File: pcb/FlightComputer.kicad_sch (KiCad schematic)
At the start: 79 parts, among them J1 USB4105-GF-A, J2 MOTOR L, J3 MOTOR R, J4 LED L, J7 SERVO R, J8 SERVO R, Q1 DMG3415U, Q2 Si2319CDS, Q3 Si2319CDS, Q4 MMBT3904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

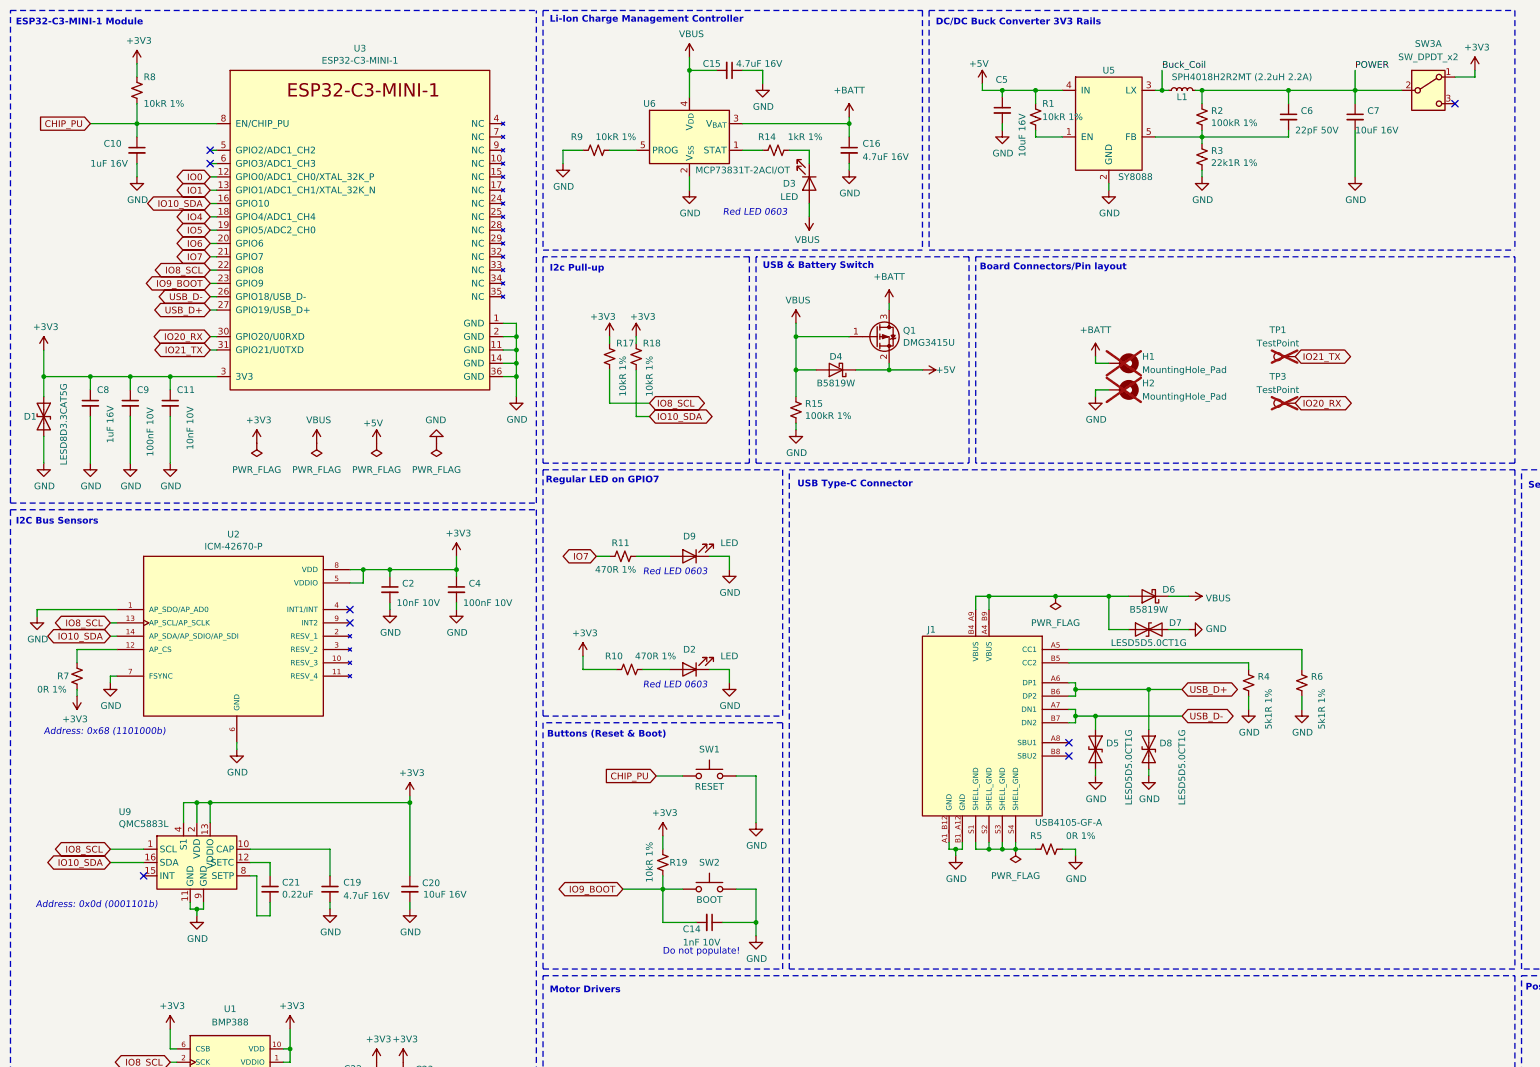
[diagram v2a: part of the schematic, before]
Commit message: Correct switch symbol to reduce warnings
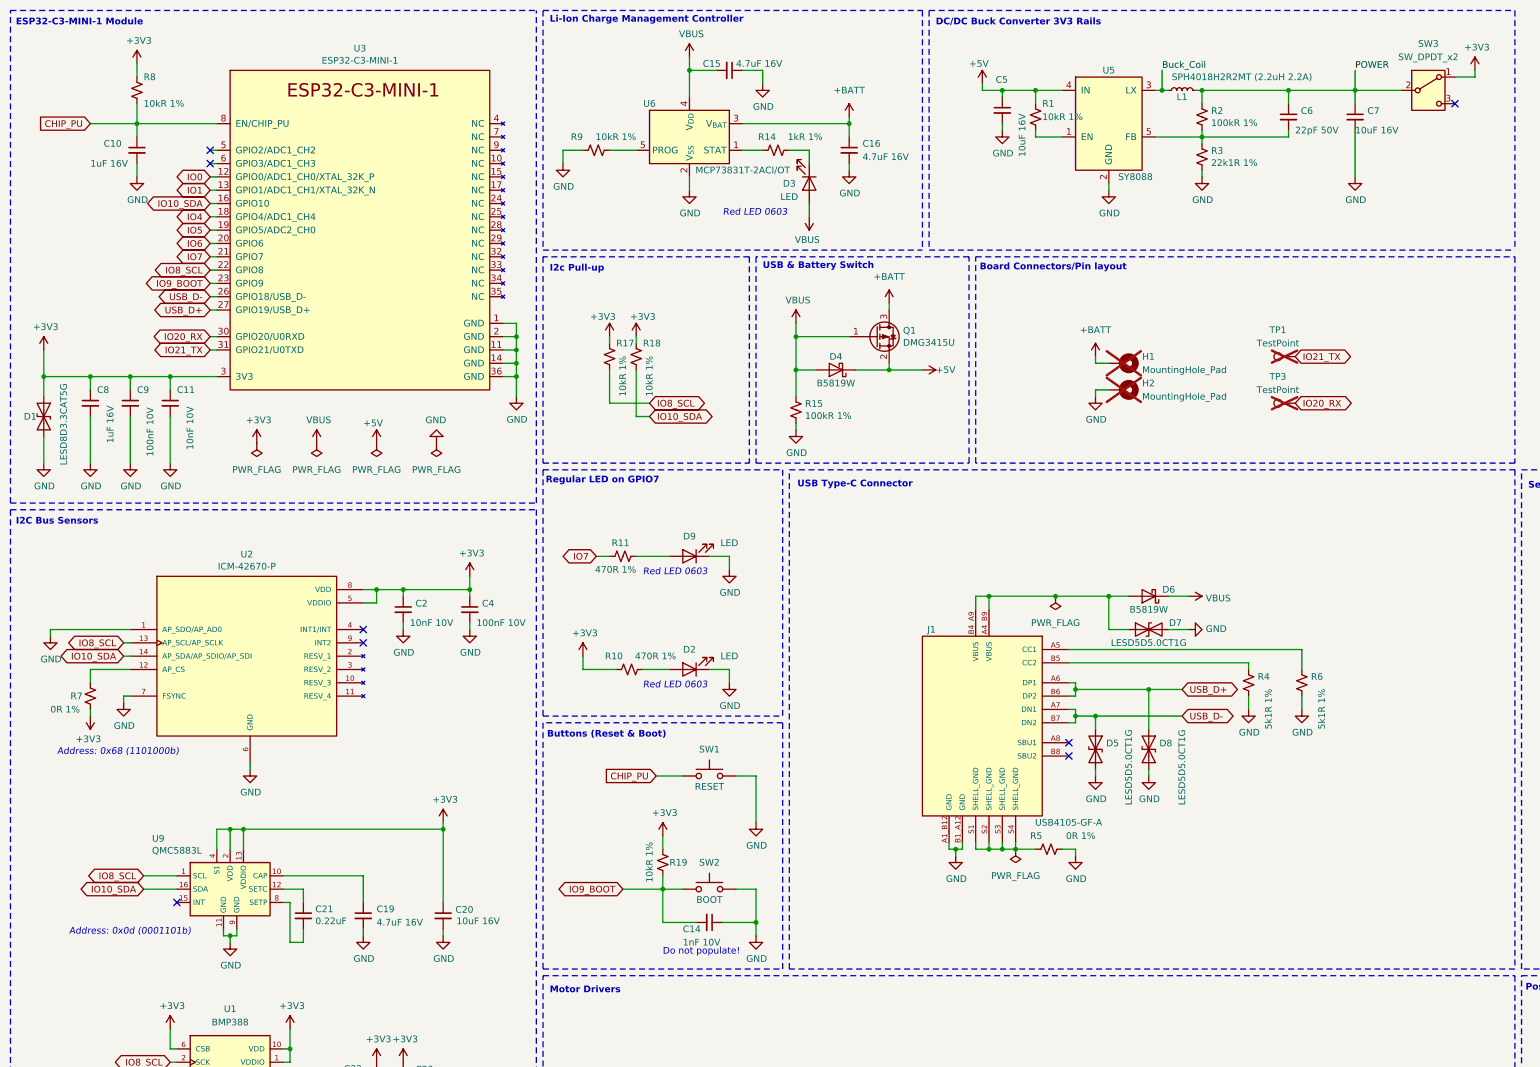
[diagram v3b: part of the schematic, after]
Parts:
- SW3: symbol Switch:SW_DPDT_x2 -> Switch:SW_SPDT
- U1: LCSC (none) -> C779278
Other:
- moved on the sheet: C19, C2, C20, C21, C4, R7, U2, U9

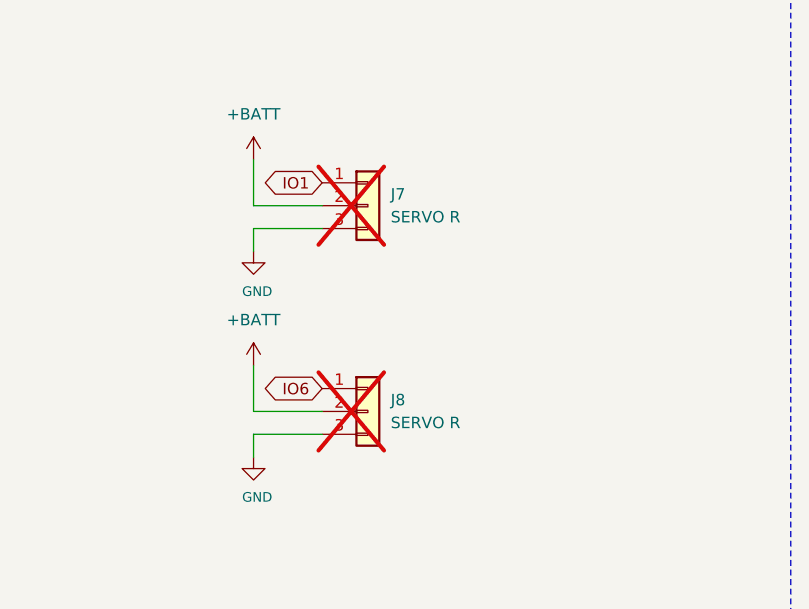
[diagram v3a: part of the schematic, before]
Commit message: Rotate servos pinouts
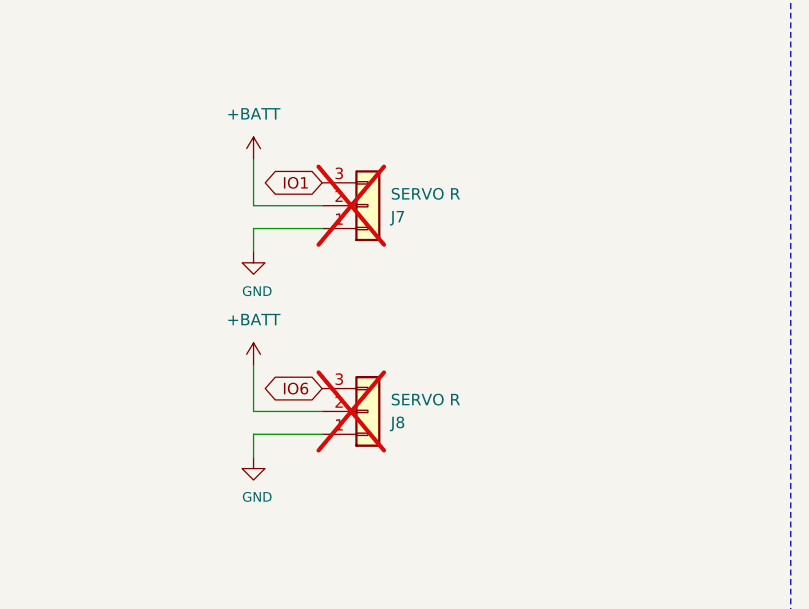
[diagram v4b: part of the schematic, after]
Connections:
- net GND: now also J7.1 (Pin_1), J8.1 (Pin_1); no longer J7.3 (Pin_3), J8.3 (Pin_3)
- net IO1: now also J7.3 (Pin_3); no longer J7.1 (Pin_1)
- net IO6: now also J8.3 (Pin_3); no longer J8.1 (Pin_1)
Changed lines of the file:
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@@
 		(lib_id "Connector_Generic:Conn_01x03")
 		(at 358.14 165.1 0)
+		(mirror x)
 		(unit 1)
 		(exclude_from_sim no)
@@
 		(fields_autoplaced yes)
 		(property "Reference" "J8"
-			(at 360.68 163.8299 0)
+			(at 360.68 166.3701 0)
 			(effects
 				(font
@@
 		)
 		(property "Value" "SERVO R"
-			(at 360.68 166.3699 0)
+			(at 360.68 163.8301 0)
 			(effects
 				(font
@@
 		(lib_id "Connector_Generic:Conn_01x03")
 		(at 358.14 142.24 0)
+		(mirror x)
 		(unit 1)
 		(exclude_from_sim no)
@@
 		(fields_autoplaced yes)
 		(property "Reference" "J7"
-			(at 360.68 140.9699 0)
+			(at 360.68 143.5101 0)
 			(effects
 				(font
@@
 		)
 		(property "Value" "SERVO R"
-			(at 360.68 143.5099 0)
+			(at 360.68 140.9701 0)
 			(effects
 				(font

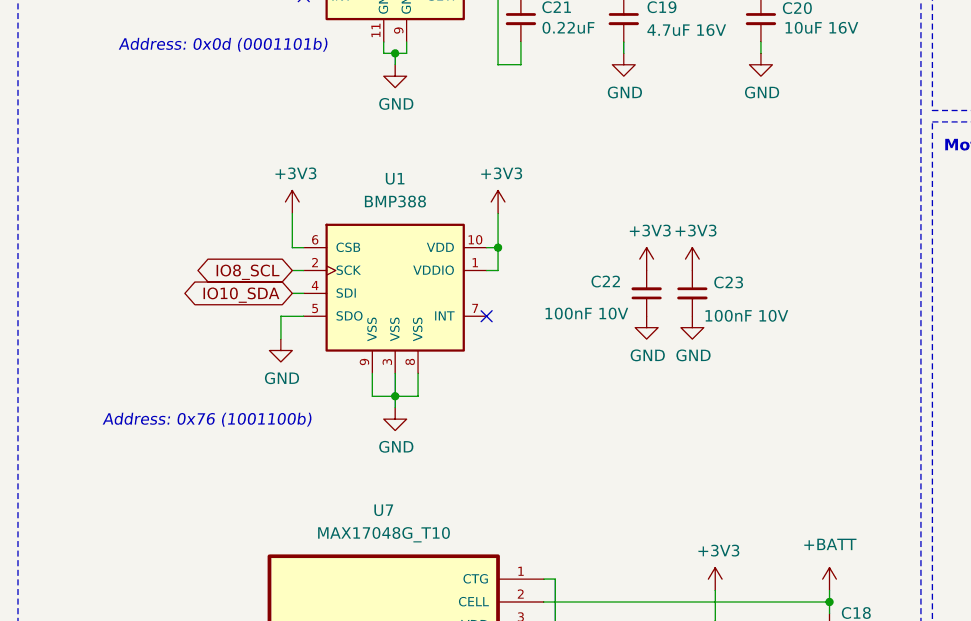
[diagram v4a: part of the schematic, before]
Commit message: Remove barometer
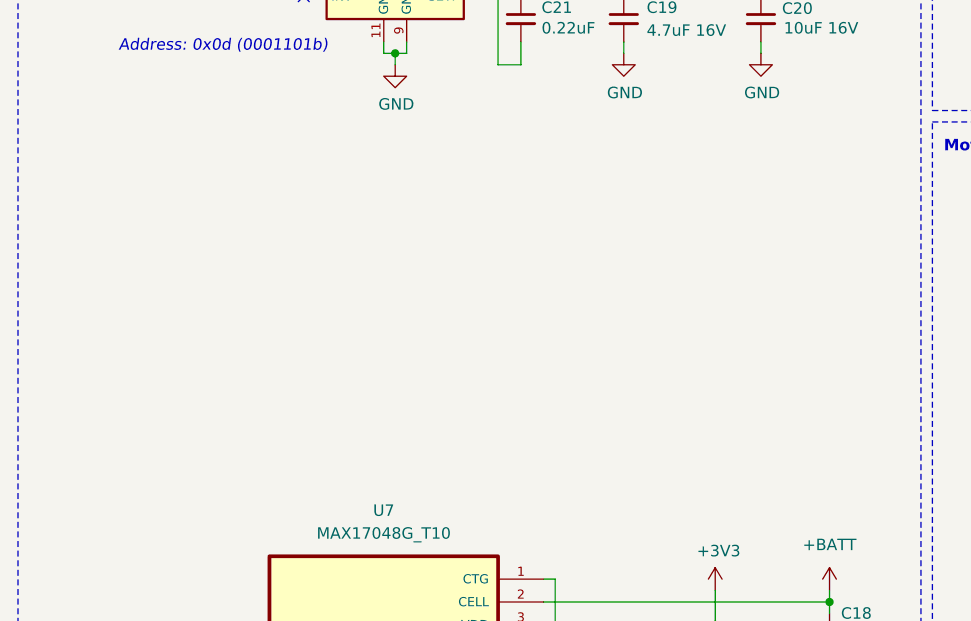
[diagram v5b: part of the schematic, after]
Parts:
- removed C22, C23: 100nF 10V, Capacitor_SMD:C_0402_1005Metric, symbol Device:C_Small
- removed U1: BMP388, Package_LGA:Rohm_MLGA010V020A_LGA-10_2x2mm_P0.45mm_LayoutBorder2x3y, symbol Rust_Board:BMP388
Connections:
- no-connect marks 10 -> 9
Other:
- note removed: "Address: 0x76 (1001100b)"

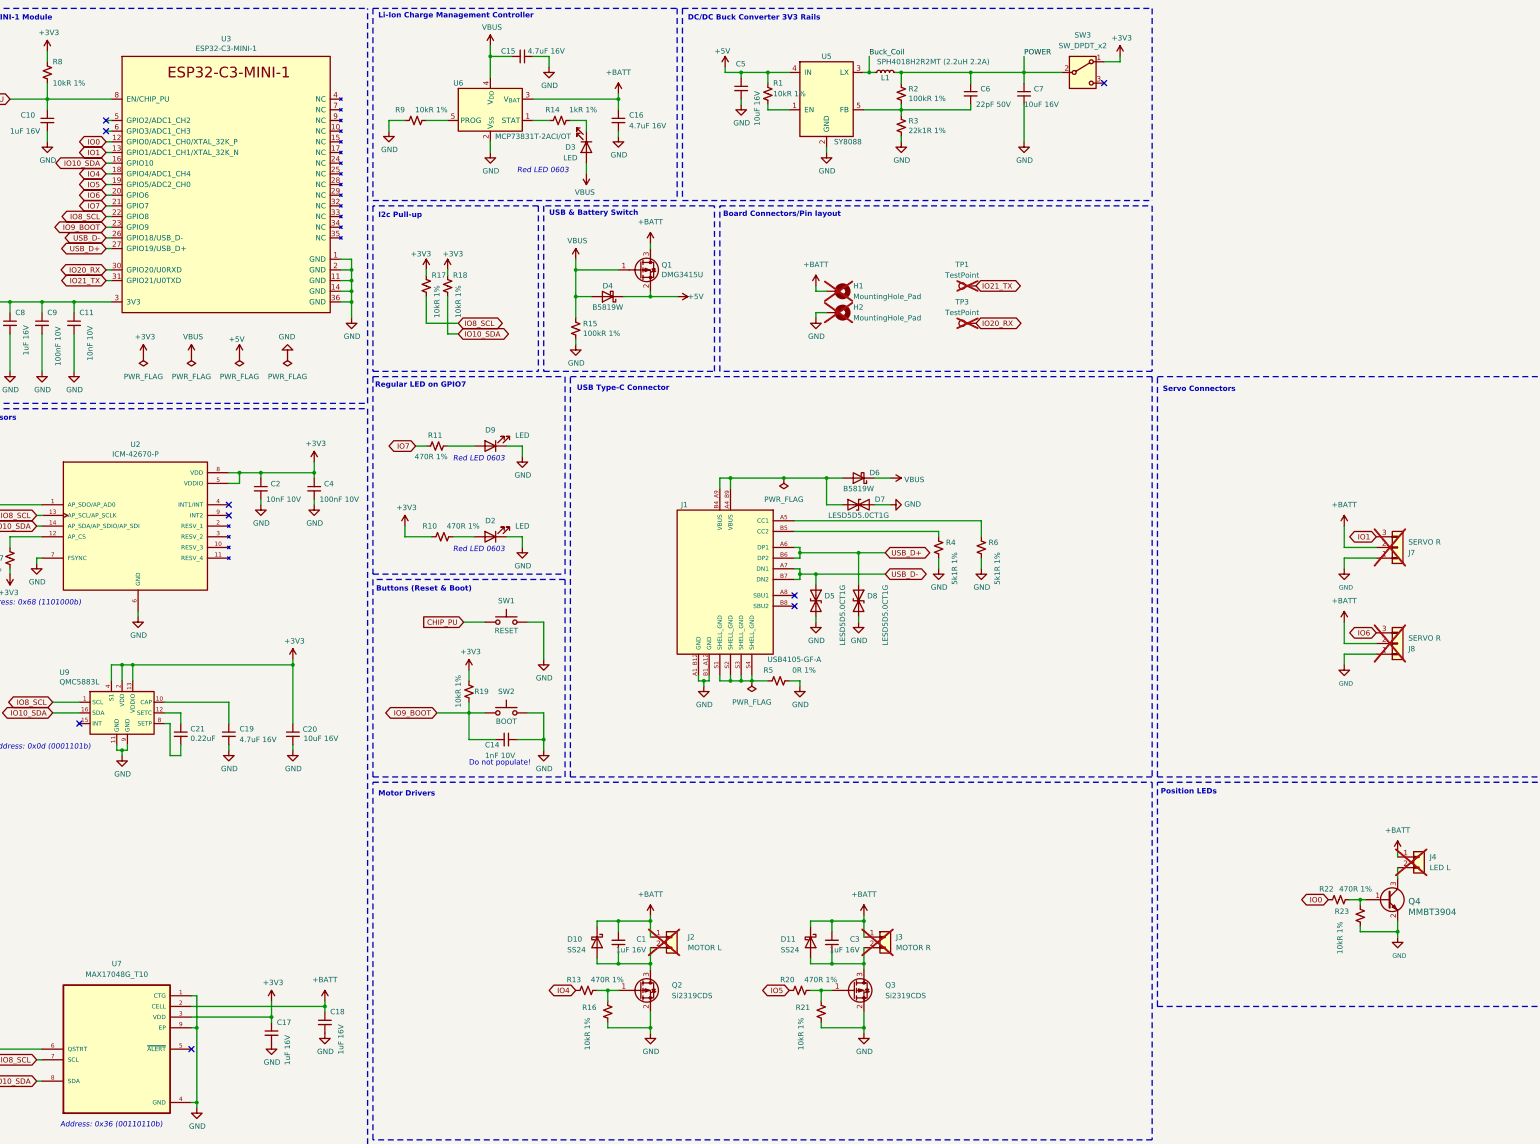
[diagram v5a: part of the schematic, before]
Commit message: Reduce board size
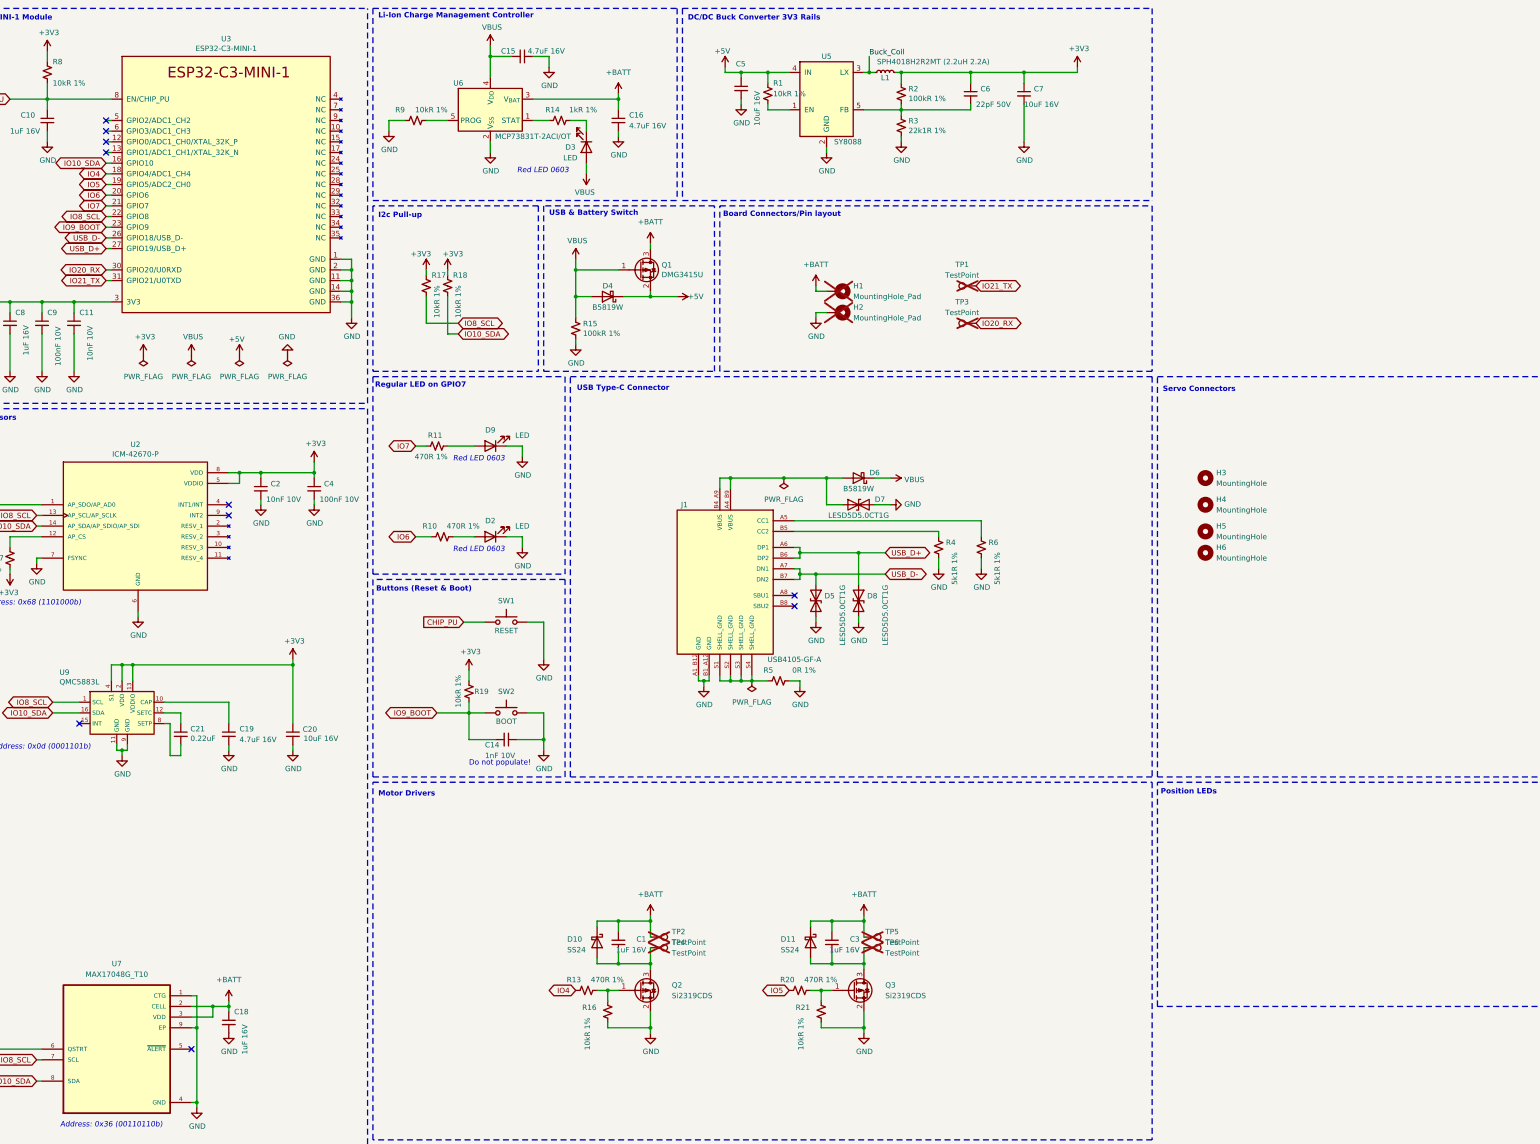
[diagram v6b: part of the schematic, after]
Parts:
- removed C17: 1uF 16V, Capacitor_SMD:C_0402_1005Metric, symbol Device:C_Small
- removed J2: MOTOR L, Connector_PinHeader_2.00mm:PinHeader_1x02_P2.00mm_Vertical, symbol Connector_Generic:Conn_01x02
- removed J3: MOTOR R, Connector_PinHeader_2.00mm:PinHeader_1x02_P2.00mm_Vertical, symbol Connector_Generic:Conn_01x02
- removed J4: LED L, Connector_PinHeader_2.00mm:PinHeader_1x02_P2.00mm_Vertical, symbol Connector_Generic:Conn_01x02
- removed J7, J8: SERVO R, Connector_PinSocket_2.00mm:PinSocket_1x03_P2.00mm_Vertical, symbol Connector_Generic:Conn_01x03
- removed Q4: MMBT3904, Package_TO_SOT_SMD:SOT-23, symbol Transistor_BJT:MMBT3904
- removed R22: 470R 1%, Resistor_SMD:R_0402_1005Metric, symbol Device:R_Small_US
- removed R23: 10kR 1%, Resistor_SMD:R_0402_1005Metric, symbol Device:R_Small_US
- removed SW3: SW_DPDT_x2, Rust_Board:SW_SPDT_PCM12, symbol Switch:SW_SPDT
- added H3, H4, H5, H6: MountingHole, MountingHole:MountingHole_2.2mm_M2_DIN965, symbol Mechanical:MountingHole
- added TP2, TP4, TP5, TP6: TestPoint, TestPoint:TestPoint_Pad_D2.0mm, symbol Connector:TestPoint
- H1, H2: footprint TestPoint:TestPoint_Keystone_5005-5009_Compact -> TestPoint:TestPoint_Pad_D2.0mm
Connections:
- net POWER is gone; now on net +3V3: C6.1, C7.1, L1.2, R2.1
- net +3V3: no longer R10.1, U7.3 (VDD)
- net +BATT: now also U7.3 (VDD), TP2.1, TP5.1
- net IO6: now also R10.1
- net at C1.1, D10.2 (A), Q2.3 (D): now also TP4.1
- net at C3.1, D11.2 (A), Q3.3 (D): now also TP6.1
- net IO0: no longer names the net of U3.12 (GPIO0/ADC1_CH0/XTAL_32K_P)
- net IO1: no longer names the net of U3.13 (GPIO1/ADC1_CH1/XTAL_32K_N)
- no-connect marks 9 -> 10
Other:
- moved on the sheet: C18
